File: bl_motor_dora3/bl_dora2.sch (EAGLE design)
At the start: 78 parts

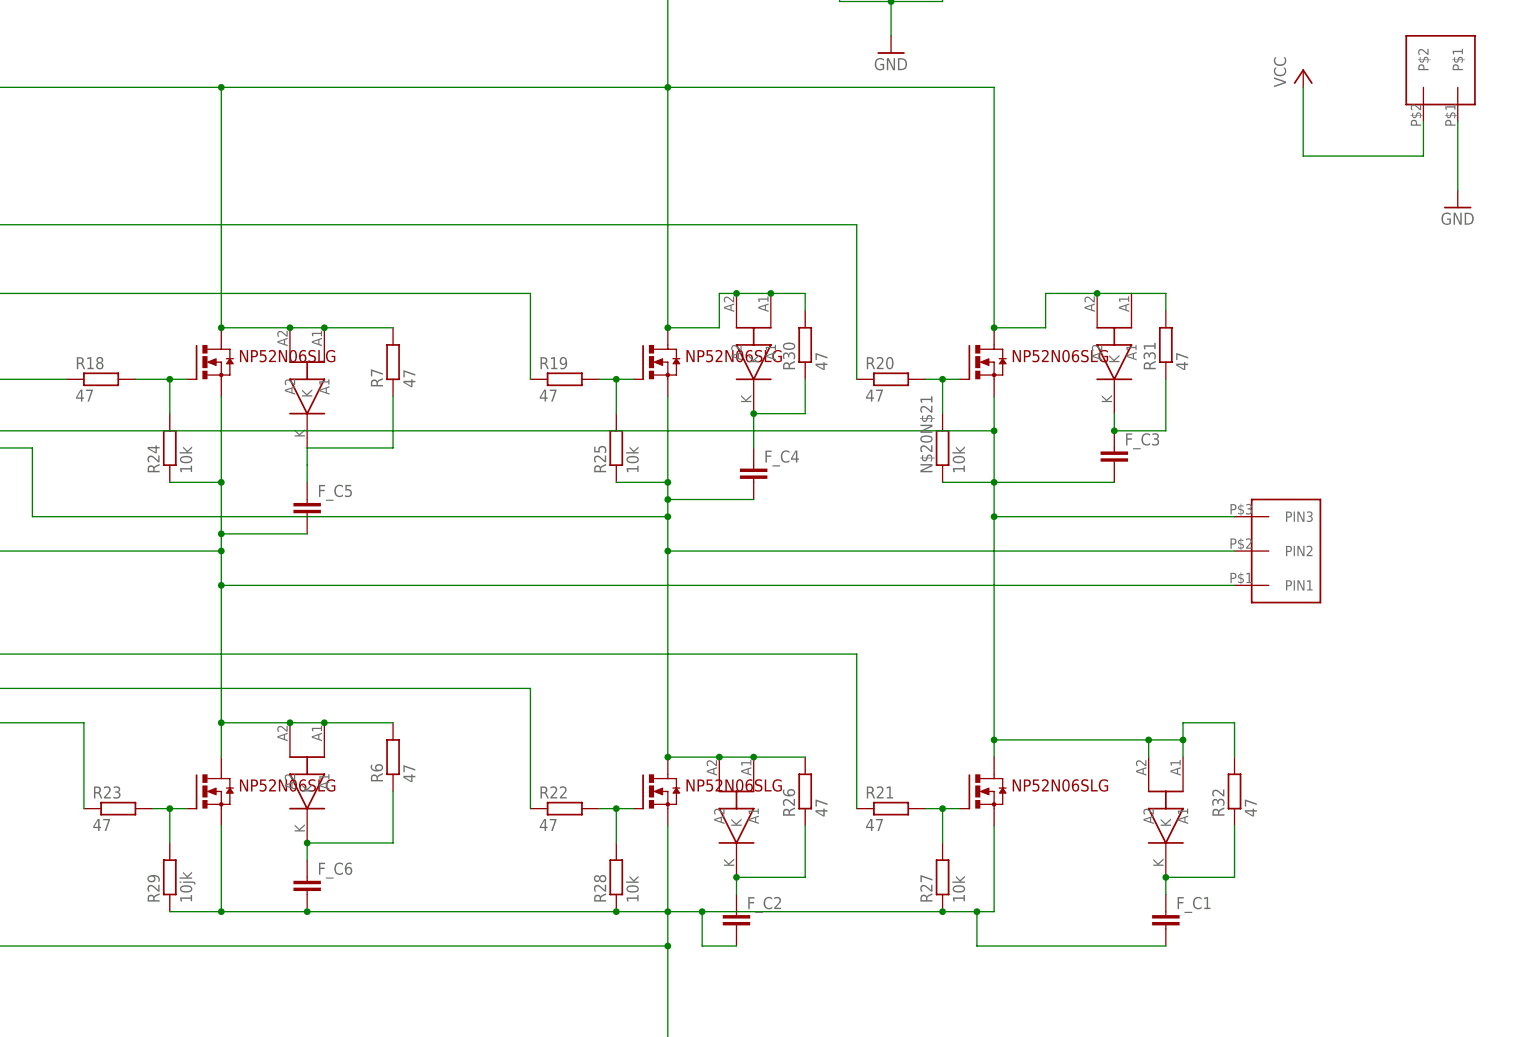
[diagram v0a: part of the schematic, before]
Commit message: 一応完成したもの
fetにスナバ回路を加えることによりモーターサージを吸収できるようにした。ゲート・ソース間にコンデンサを入れられるようにして、セルフターンオンしないように細かく調整できるようにした。デッドタイムの設計を変え忘れた。確か47kΩでデッドタイムが700nSecほどになる。空冷するためのファン用のコネクタを追加した。還流ダイオードを入れるスペースが作れなかった。この設計で実験し思う性能が出せない場合は基板サイズを犠牲にするか4層化し、知っている限りの保護回路をマシマシにする。
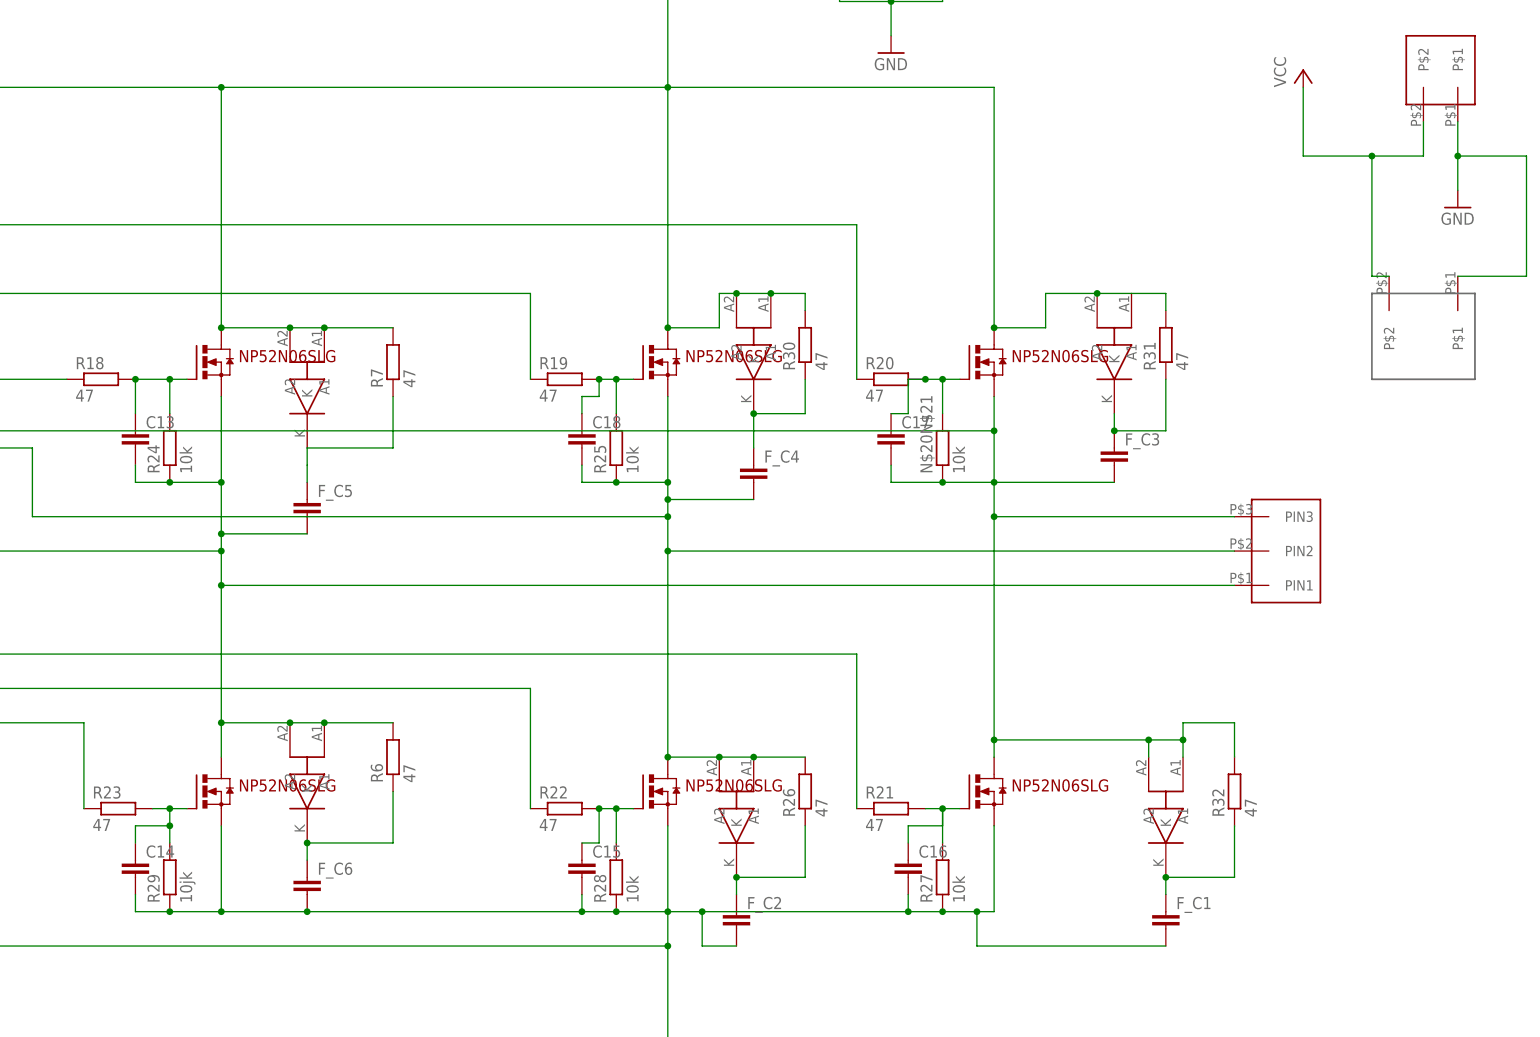
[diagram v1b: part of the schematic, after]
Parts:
- added C13, C14, C15, C16, C17, C18: (no value), rcl:C-EUC2012
- added U$19: XH_2P, user:XH_2P
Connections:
- net GND: now also U$19.P$1
- net N$19: now also C13.2
- net N$25: now also C13.1
- net N$26: now also C18.1
- net N$27: now also C17.1
- net N$28: now also C16.1
- net N$29: now also C15.1
- net N$30: now also C14.1
- net N$4: now also C17.2
- net N$50: now also C18.2
- net N$8: now also C14.2, C15.2, C16.2
- net VCC: now also U$19.P$2
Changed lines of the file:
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@@
 <part name="R31" library="rcl" library_urn="urn:adsk.eagle:library:334" deviceset="R-EU_" device="R2512" package3d_urn="urn:adsk.eagle:package:23545/2" value="47"/>
 <part name="R32" library="rcl" library_urn="urn:adsk.eagle:library:334" deviceset="R-EU_" device="R2512" package3d_urn="urn:adsk.eagle:package:23545/2" value="47"/>
+<part name="U$19" library="user" deviceset="XH_2P" device=""/>
+<part name="C13" library="rcl" library_urn="urn:adsk.eagle:library:334" deviceset="C-EU" device="C2012" package3d_urn="urn:adsk.eagle:package:23625/2"/>
+<part name="C14" library="rcl" library_urn="urn:adsk.eagle:library:334" deviceset="C-EU" device="C2012" package3d_urn="urn:adsk.eagle:package:23625/2"/>
+<part name="C15" library="rcl" library_urn="urn:adsk.eagle:library:334" deviceset="C-EU" device="C2012" package3d_urn="urn:adsk.eagle:package:23625/2"/>
+<part name="C16" library="rcl" library_urn="urn:adsk.eagle:library:334" deviceset="C-EU" device="C2012" package3d_urn="urn:adsk.eagle:package:23625/2"/>
+<part name="C17" library="rcl" library_urn="urn:adsk.eagle:library:334" deviceset="C-EU" device="C2012" package3d_urn="urn:adsk.eagle:package:23625/2"/>
+<part name="C18" library="rcl" library_urn="urn:adsk.eagle:library:334" deviceset="C-EU" device="C2012" package3d_urn="urn:adsk.eagle:package:23625/2"/>
 </parts>
 <sheets>
@@
 <attribute name="VALUE" x="468.122" y="59.69" size="1.778" layer="96" rot="R90"/>
 </instance>
+<instance part="U$19" gate="G$1" x="492.76" y="134.62" smashed="yes" rot="R270"/>
+<instance part="C13" gate="G$1" x="302.26" y="116.84" smashed="yes">
+<attribute name="NAME" x="303.784" y="117.221" size="1.778" layer="95"/>
+<attribute name="VALUE" x="303.784" y="112.141" size="1.778" layer="96"/>
+</instance>
+<instance part="C14" gate="G$1" x="302.26" y="53.34" smashed="yes">
+<attribute name="NAME" x="303.784" y="53.721" size="1.778" layer="95"/>
+<attribute name="VALUE" x="303.784" y="48.641" size="1.778" layer="96"/>
+</instance>
+<instance part="C15" gate="G$1" x="368.3" y="53.34" smashed="yes">
+<attribute name="NAME" x="369.824" y="53.721" size="1.778" layer="95"/>
+<attribute name="VALUE" x="369.824" y="48.641" size="1.778" layer="96"/>
+</instance>
+<instance part="C16" gate="G$1" x="416.56" y="53.34" smashed="yes">
+<attribute name="NAME" x="418.084" y="53.721" size="1.778" layer="95"/>
+<attribute name="VALUE" x="418.084" y="48.641" size="1.778" layer="96"/>
+</instance>
+<instance part="C17" gate="G$1" x="414.02" y="116.84" smashed="yes">
+<attribute name="NAME" x="415.544" y="117.221" size="1.778" layer="95"/>
+<attribute name="VALUE" x="415.544" y="112.141" size="1.778" layer="96"/>
+</instance>
+<instance part="C18" gate="G$1" x="368.3" y="116.84" smashed="yes">
+<attribute name="NAME" x="369.824" y="117.221" size="1.778" layer="95"/>
+<attribute name="VALUE" x="369.824" y="112.141" size="1.778" layer="96"/>
+</instance>
 </instances>
 <busses>
@@
 </segment>
 <segment>
-<wire x1="497.84" y1="162.56" x2="497.84" y2="152.4" width="0.1524" layer="91"/>
+<wire x1="497.84" y1="162.56" x2="497.84" y2="157.48" width="0.1524" layer="91"/>
 <pinref part="GND1" gate="1" pin="GND"/>
 <pinref part="U$24" gate="G$1" pin="P$1"/>
+<wire x1="497.84" y1="157.48" x2="497.84" y2="152.4" width="0.1524" layer="91"/>
+<wire x1="497.84" y1="157.48" x2="508" y2="157.48" width="0.1524" layer="91"/>
+<junction x="497.84" y="157.48"/>
+<wire x1="508" y1="157.48" x2="508" y2="139.7" width="0.1524" layer="91"/>
+<pinref part="U$19" gate="G$1" pin="P$1"/>
+<wire x1="508" y1="139.7" x2="497.84" y2="139.7" width="0.1524" layer="91"/>
 </segment>
 </net>
@@
 <segment>
 <wire x1="492.76" y1="162.56" x2="492.76" y2="157.48" width="0.1524" layer="91"/>
-<wire x1="492.76" y1="157.48" x2="474.98" y2="157.48" width="0.1524" layer="91"/>
+<wire x1="492.76" y1="157.48" x2="485.14" y2="157.48" width="0.1524" layer="91"/>
+<wire x1="485.14" y1="157.48" x2="474.98" y2="157.48" width="0.1524" layer="91"/>
 <wire x1="474.98" y1="157.48" x2="474.98" y2="167.64" width="0.1524" layer="91"/>
 <pinref part="P+4" gate="VCC" pin="VCC"/>
 <pinref part="U$24" gate="G$1" pin="P$2"/>
+<pinref part="U$19" gate="G$1" pin="P$2"/>
+<wire x1="485.14" y1="157.48" x2="485.14" y2="139.7" width="0.1524" layer="91"/>
+<wire x1="485.14" y1="139.7" x2="487.68" y2="139.7" width="0.1524" layer="91"/>
+<junction x="485.14" y="157.48"/>
 </segment>
 </net>
@@
 <pinref part="R27" gate="G$1" pin="1"/>
 <wire x1="314.96" y1="45.72" x2="327.66" y2="45.72" width="0.1524" layer="91"/>
-<wire x1="327.66" y1="45.72" x2="373.38" y2="45.72" width="0.1524" layer="91"/>
+<wire x1="327.66" y1="45.72" x2="368.3" y2="45.72" width="0.1524" layer="91"/>
+<wire x1="368.3" y1="45.72" x2="373.38" y2="45.72" width="0.1524" layer="91"/>
 <wire x1="373.38" y1="45.72" x2="381" y2="45.72" width="0.1524" layer="91"/>
 <junction x="373.38" y="45.72"/>
@@
 <junction x="314.96" y="45.72"/>
 <pinref part="U$10" gate="G$1" pin="PIN3_S"/>
-<wire x1="386.08" y1="45.72" x2="421.64" y2="45.72" width="0.1524" layer="91"/>
+<wire x1="386.08" y1="45.72" x2="416.56" y2="45.72" width="0.1524" layer="91"/>
+<wire x1="416.56" y1="45.72" x2="421.64" y2="45.72" width="0.1524" layer="91"/>
 <wire x1="314.96" y1="58.42" x2="314.96" y2="45.72" width="0.1524" layer="91"/>
 <junction x="381" y="45.72"/>
@@
 <wire x1="426.72" y1="40.64" x2="426.72" y2="45.72" width="0.1524" layer="91"/>
 <junction x="426.72" y="45.72"/>
+<pinref part="C15" gate="G$1" pin="2"/>
+<wire x1="368.3" y1="48.26" x2="368.3" y2="45.72" width="0.1524" layer="91"/>
+<junction x="368.3" y="45.72"/>
+<pinref part="C14" gate="G$1" pin="2"/>
+<wire x1="302.26" y1="48.26" x2="302.26" y2="45.72" width="0.1524" layer="91"/>
+<wire x1="302.26" y1="45.72" x2="307.34" y2="45.72" width="0.1524" layer="91"/>
+<junction x="307.34" y="45.72"/>
+<pinref part="C16" gate="G$1" pin="2"/>
+<wire x1="416.56" y1="48.26" x2="416.56" y2="45.72" width="0.1524" layer="91"/>
+<junction x="416.56" y="45.72"/>
 </segment>
 </net>
@@
 <wire x1="340.36" y1="73.66" x2="330.2" y2="73.66" width="0.1524" layer="91"/>
 <junction x="330.2" y="73.66"/>
+<pinref part="C13" gate="G$1" pin="2"/>
+<wire x1="302.26" y1="111.76" x2="302.26" y2="109.22" width="0.1524" layer="91"/>
+<wire x1="302.26" y1="109.22" x2="307.34" y2="109.22" width="0.1524" layer="91"/>
+<junction x="307.34" y="109.22"/>
 </segment>
 </net>
@@
 <wire x1="307.34" y1="119.38" x2="307.34" y2="124.46" width="0.1524" layer="91"/>
 <junction x="307.34" y="124.46"/>
+<pinref part="C13" gate="G$1" pin="1"/>
+<wire x1="302.26" y1="119.38" x2="302.26" y2="124.46" width="0.1524" layer="91"/>
+<junction x="302.26" y="124.46"/>
 </segment>
 </net>
@@
 <wire x1="373.38" y1="119.38" x2="373.38" y2="124.46" width="0.1524" layer="91"/>
 <junction x="373.38" y="124.46"/>
+<pinref part="C18" gate="G$1" pin="1"/>
+<wire x1="368.3" y1="119.38" x2="368.3" y2="121.92" width="0.1524" layer="91"/>
+<wire x1="368.3" y1="121.92" x2="370.84" y2="121.92" width="0.1524" layer="91"/>
+<wire x1="370.84" y1="121.92" x2="370.84" y2="124.46" width="0.1524" layer="91"/>
+<junction x="370.84" y="124.46"/>
 </segment>
 </net>
@@
 <wire x1="421.64" y1="119.38" x2="421.64" y2="124.46" width="0.1524" layer="91"/>
 <junction x="421.64" y="124.46"/>
+<pinref part="C17" gate="G$1" pin="1"/>
+<wire x1="414.02" y1="119.38" x2="416.56" y2="119.38" width="0.1524" layer="91"/>
+<wire x1="416.56" y1="119.38" x2="416.56" y2="124.46" width="0.1524" layer="91"/>
+<wire x1="416.56" y1="124.46" x2="419.1" y2="124.46" width="0.1524" layer="91"/>
+<junction x="419.1" y="124.46"/>
 </segment>
 </net>
@@
 <wire x1="421.64" y1="55.88" x2="421.64" y2="60.96" width="0.1524" layer="91"/>
 <junction x="421.64" y="60.96"/>
+<pinref part="C16" gate="G$1" pin="1"/>
+<wire x1="416.56" y1="55.88" x2="416.56" y2="58.42" width="0.1524" layer="91"/>
+<wire x1="416.56" y1="58.42" x2="421.64" y2="58.42" width="0.1524" layer="91"/>
+<wire x1="421.64" y1="58.42" x2="421.64" y2="60.96" width="0.1524" layer="91"/>
 </segment>
 </net>
@@
 <wire x1="373.38" y1="55.88" x2="373.38" y2="60.96" width="0.1524" layer="91"/>
 <junction x="373.38" y="60.96"/>
+<pinref part="C15" gate="G$1" pin="1"/>
+<wire x1="368.3" y1="55.88" x2="370.84" y2="55.88" width="0.1524" layer="91"/>
+<wire x1="370.84" y1="55.88" x2="370.84" y2="60.96" width="0.1524" layer="91"/>
+<junction x="370.84" y="60.96"/>
 </segment>
 </net>
@@
 <pinref part="R29" gate="G$1" pin="2"/>
 <wire x1="307.34" y1="60.96" x2="304.8" y2="60.96" width="0.1524" layer="91"/>
-<wire x1="307.34" y1="55.88" x2="307.34" y2="60.96" width="0.1524" layer="91"/>
+<wire x1="307.34" y1="55.88" x2="307.34" y2="58.42" width="0.1524" layer="91"/>
 <junction x="307.34" y="60.96"/>
+<pinref part="C14" gate="G$1" pin="1"/>
+<wire x1="307.34" y1="58.42" x2="307.34" y2="60.96" width="0.1524" layer="91"/>
+<wire x1="302.26" y1="55.88" x2="302.26" y2="58.42" width="0.1524" layer="91"/>
+<wire x1="302.26" y1="58.42" x2="307.34" y2="58.42" width="0.1524" layer="91"/>
+<junction x="307.34" y="58.42"/>
 </segment>
 </net>
@@
 <wire x1="457.2" y1="73.66" x2="457.2" y2="71.12" width="0.1524" layer="91"/>
 <junction x="457.2" y="71.12"/>
+<pinref part="C17" gate="G$1" pin="2"/>
+<wire x1="414.02" y1="111.76" x2="414.02" y2="109.22" width="0.1524" layer="91"/>
+<wire x1="414.02" y1="109.22" x2="421.64" y2="109.22" width="0.1524" layer="91"/>
+<junction x="421.64" y="109.22"/>
 </segment>
 </net>
@@
 <junction x="388.62" y="68.58"/>
 <junction x="381" y="68.58"/>
-</segment>
-</net>
+<pinref part="C18" gate="G$1" pin="2"/>
+<wire x1="368.3" y1="111.76" x2="368.3" y2="109.22" width="0.1524" layer="91"/>
+<wire x1="368.3" y1="109.22" x2="373.38" y2="109.22" width="0.1524" layer="91"/>
+<junction x="373.38" y="109.22"/>
+</segment>
+</net>

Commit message: フィードバックを受けて修正したもの
スナバを大幅に修正して非放電型スナバにした。これにより抵抗器の損失を少なくできるため小型の抵抗器が使えるようになった。スナバに使っていたダイオードを還流ダイオードに使用して、スナバのダイオードは小さめのものに変えた。電流センサ用の配線をくねくねしないで揃うように頑張った。非放電型スナバの周りの配線が複雑になって怪しい気がするのでチェックお願いします。
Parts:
- added R33, R34: 0, user:1608REG
- added U$20, U$21, U$22, U$26, U$27, U$28: ES3BB13F, user:ES3BB13F
- C13, C14, C15, C16, C17, C18: value (none) -> 5n
- C5, C6, C7: value 0.1u -> 0.22u
- R15: value 100k -> 33k
- R18, R19, R20, R21, R22, R23: value 47 -> 10
- R26, R30, R31, R32, R6, R7: device rcl:R-EU_R2512 -> rcl:R-EU_R1206
- R29: value 10jk -> 10k
- R3, R4: value 4.7k -> 10k
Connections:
- removed net N$39: F_C1.1, R32.1, U$18.K
- removed net N$4: C17.2, C5.2, F_C3.2, N$20N$21.1, R32.2, U$1.PIN25_SC, U$11.PIN3_S, U$12.PIN2_D, U$18.A1, U$18.A2, U$25.PIN3
- removed net N$8: C14.2, C15.2, C16.2, F_C1.2, F_C2.2, F_C6.2, R11.2, R12.2, R13.2, R14.2, R27.1, R28.1, R29.1, U$1.PIN21_CSN, U$1.PIN38_LSS, U$10.PIN3_S, U$12.PIN3_S, U$8.PIN3_S
- removed net N$9: F_C6.1, R6.1, U$14.K
- new net N$10: R33.2, U$1.PIN22_CSP
- new net N$20: R34.2, U$1.PIN21_CSN
- new net N$41: F_C3.2, R30.2, U$22.A
- new net N$44: C17.2, C5.2, N$20N$21.1, U$1.PIN25_SC, U$11.PIN3_S, U$12.PIN2_D, U$17.A1, U$17.A2, U$18.K, U$22.C, U$25.PIN3, U$28.A
- new net N$45: F_C1.1, R26.1, U$28.C
- new net N$47: F_C2.1, R7.1, U$27.C
- net GND: now also R34.1; no longer U$1.PIN22_CSP
- net N$19: now also U$13.A1, U$13.A2, U$14.K, U$20.C, U$26.A; no longer F_C5.2, R6.2, U$14.A1, U$14.A2
- net N$38: now also F_C4.2, R31.2, U$21.A; no longer F_C2.1, R26.1, U$15.K
- net N$40: now also C14.2, C15.2, C16.2, F_C1.2, F_C2.2, F_C6.2, R11.2, R12.2, R13.2, R14.2, R27.1, R28.1, R29.1, R30.1, R32.1, R33.1, U$1.PIN38_LSS, U$10.PIN3_S, U$12.PIN3_S, U$14.A1, U$14.A2, U$15.A1, U$15.A2, U$18.A1, U$18.A2, U$8.PIN3_S; no longer F_C3.1, U$17.K
- net N$42: now also F_C6.1, R6.1, U$26.C; no longer F_C4.1, R30.1, U$16.K
- net N$5: now also F_C5.2, R32.2, U$20.A; no longer F_C5.1, R7.1, U$13.K
- net N$50: now also U$15.K, U$16.A1, U$16.A2, U$21.C, U$27.A; no longer F_C4.2, R26.2, U$15.A1, U$15.A2
- net VCC: now also F_C3.1, F_C4.1, F_C5.1, R26.2, R6.2, U$13.K, U$16.K, U$17.K; no longer R30.2, R31.2, U$13.A1, U$13.A2, U$16.A1, U$16.A2, U$17.A1, U$17.A2
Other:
- note added: "47Ωの抵抗器は1206の0.66W。rs品番721-9715"
- note added: "F_C*のコンデンサは0.1uFのフィルムコンデンサ"
- note added: "csnとcspはできるだけ同じ長さで同じルート・無理にくねくねさせるなら同じながさでなくていい"
- note added: "deadタイムは約600nsec"
- note added: "fetにSQD50034ELを使う。同じto252"
- note added: "fetのドレインソース間がオン時に1Vを超えたら短絡とみなされる"
- note added: "電流制限は30Aに設定されている。refの抵抗比を変えることで変更可"
- note removed: "csnとcspはできるだけ同じ長さで同じルート"
- note removed: "deadタイムは約1420nsec"
- moved on the sheet: C13, C14, C15, C16, C17, C18, F_C2, F_C3, F_C4, F_C5, F_C6, R10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
